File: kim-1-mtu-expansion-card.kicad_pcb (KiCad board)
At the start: 2 copper layers, 178.9 x 123.8 mm, 11 parts, among them J1 Conn_02x22_Top_Bottom, J2 Power_Connector, J3 A-J, J4 A-K, P1 KIM-1, P2 EXP_BOARD, P3 EDGE_CONN, P4 EDGE_CONN, P5 EDGE_CONN, P6 EDGE_CONN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

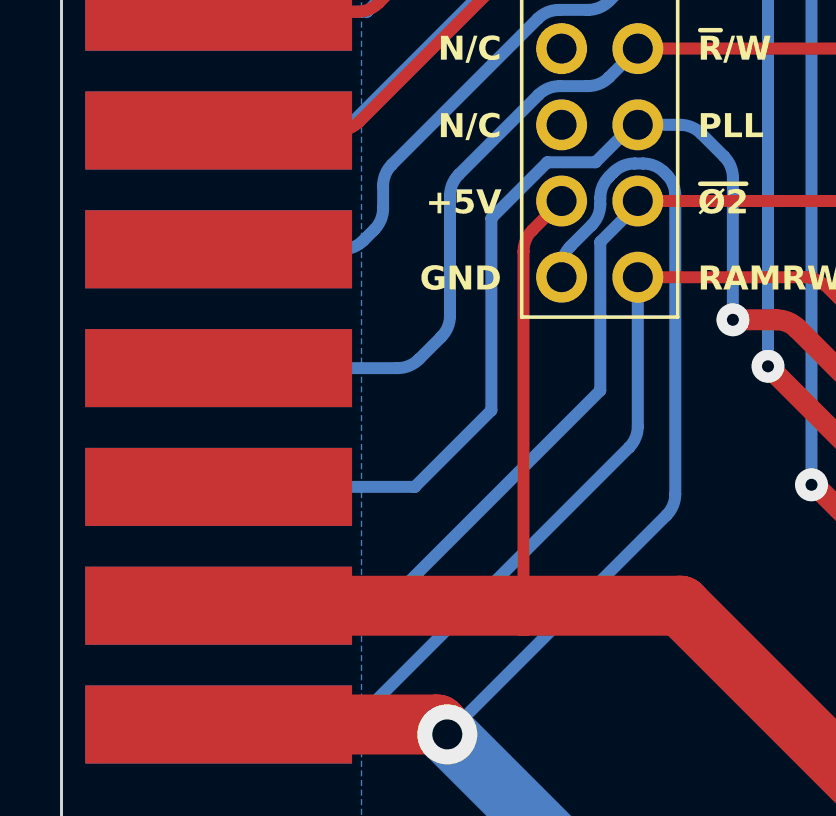
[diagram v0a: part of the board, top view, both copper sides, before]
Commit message: Thicker +5V track to pin header
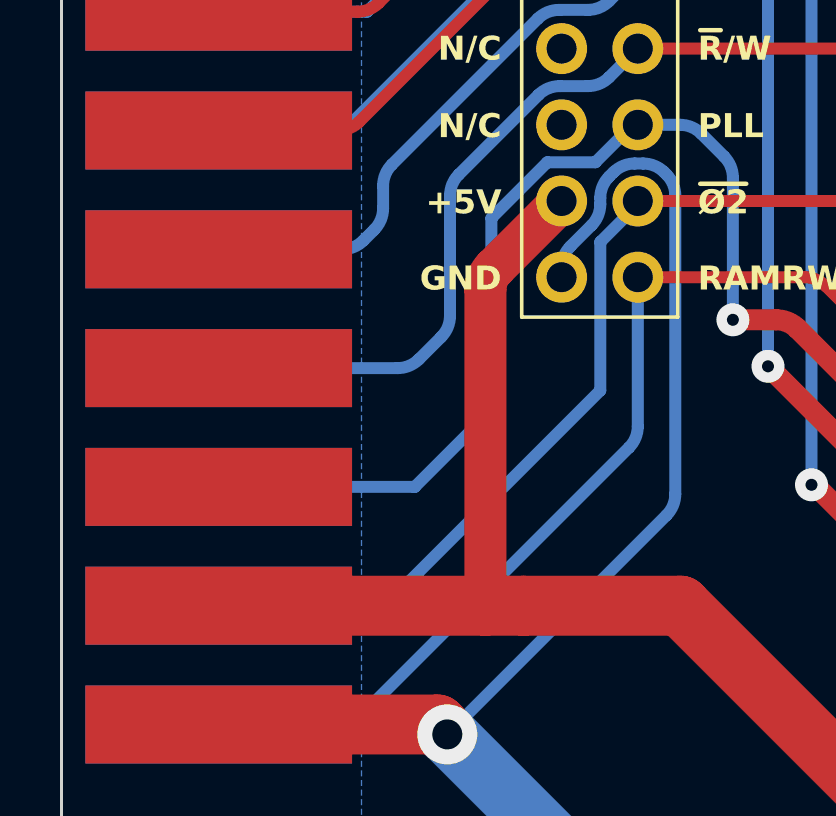
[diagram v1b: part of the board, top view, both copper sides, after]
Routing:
- net +5V: track 318.4 -> 318.9 mm
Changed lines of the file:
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@@
   (arc (start 75.995126 100.037107) (mid 75.670703 100.25388) (end 75.288019 100.33) (width 0.4) (layer "B.Cu") (net 17))
   (arc (start 77.573553 99.08) (mid 77.956236 99.15612) (end 78.28066 99.372893) (width 0.4) (layer "B.Cu") (net 17))
+  (segment (start 73.66 123.98) (end 72.39 123.98) (width 2) (layer "F.Cu") (net 21))
   (segment (start 78.895 123.98) (end 73.66 123.98) (width 2) (layer "F.Cu") (net 21))
   (segment (start 220.82 140.97) (end 218.44 140.97) (width 2) (layer "F.Cu") (net 21))
   (segment (start 95.885 140.97) (end 78.895 123.98) (width 2) (layer "F.Cu") (net 21))
+  (segment (start 74.93 110.49) (end 72.682893 112.737107) (width 1.4) (layer "F.Cu") (net 21))
   (segment (start 230.094874 123.98) (end 228.034874 121.92) (width 2) (layer "F.Cu") (net 21))
   (segment (start 233.68 123.98) (end 230.094874 123.98) (width 2) (layer "F.Cu") (net 21))
   (segment (start 228.44 148.59) (end 220.82 140.97) (width 2) (layer "F.Cu") (net 21))
-  (segment (start 73.66 112.174214) (end 73.66 123.98) (width 0.4) (layer "F.Cu") (net 21))
-  (segment (start 74.93 110.49) (end 73.952893 111.467107) (width 0.4) (layer "F.Cu") (net 21))
   (segment (start 228.034874 121.92) (end 218.44 121.92) (width 2) (layer "F.Cu") (net 21))
+  (segment (start 72.39 113.444214) (end 72.39 123.98) (width 1.4) (layer "F.Cu") (net 21))
   (segment (start 218.44 140.97) (end 95.885 140.97) (width 2) (layer "F.Cu") (net 21))
-  (segment (start 73.66 123.98) (end 63.5 123.98) (width 2) (layer "F.Cu") (net 21))
+  (segment (start 72.39 123.98) (end 63.5 123.98) (width 2) (layer "F.Cu") (net 21))
   (via (at 95.885 140.97) (size 2) (drill 1) (layers "F.Cu" "B.Cu") (net 21))
   (via (at 218.44 121.92) (size 2) (drill 1) (layers "F.Cu" "B.Cu") (net 21))
@@
   (via (at 121.285 140.97) (size 2) (drill 1) (layers "F.Cu" "B.Cu") (net 21))
   (via (at 218.44 140.97) (size 2) (drill 1) (layers "F.Cu" "B.Cu") (net 21))
-  (arc (start 73.952893 111.467107) (mid 73.73612 111.79153) (end 73.66 112.174214) (width 0.4) (layer "F.Cu") (net 21))
+  (arc (start 72.682893 112.737107) (mid 72.46612 113.06153) (end 72.39 113.444214) (width 1.4) (layer "F.Cu") (net 21))
   (segment (start 218.44 121.92) (end 218.44 140.97) (width 2) (layer "B.Cu") (net 21))
   (segment (start 125.73 123.98) (end 121.285 128.425) (width 2) (layer "B.Cu") (net 21))
